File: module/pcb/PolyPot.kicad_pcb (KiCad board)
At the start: 2 copper layers, 50 x 50 mm, 42 parts, among them J1 V_BAT_1S, J10 I2C_TEST, J2 PROG/DEBUG, J3 HUMIDITY_CONN, J4 TOF_DIST_SENS, J5 M3, J6 M3, J7 M3, J8 M3, M1 DC_WATER_PUMP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

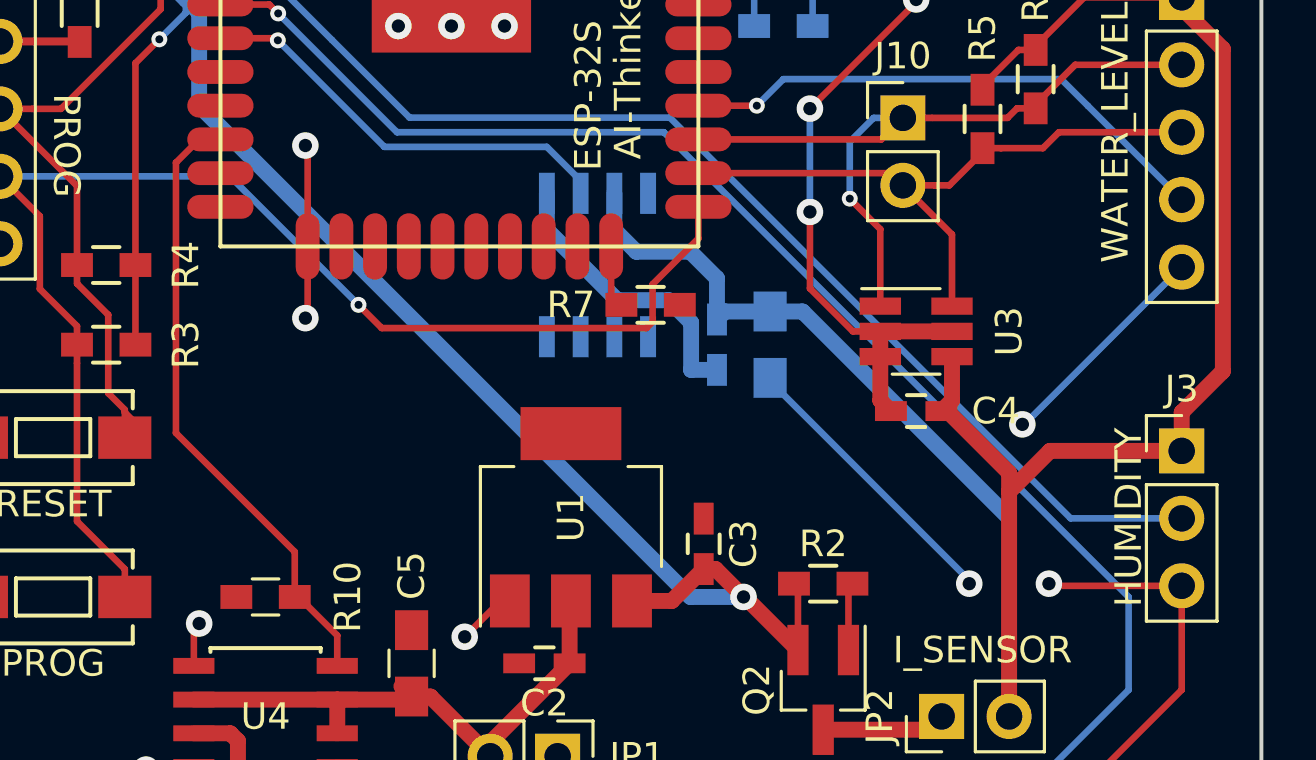
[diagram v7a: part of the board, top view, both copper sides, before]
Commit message: PCB: improve GND connection
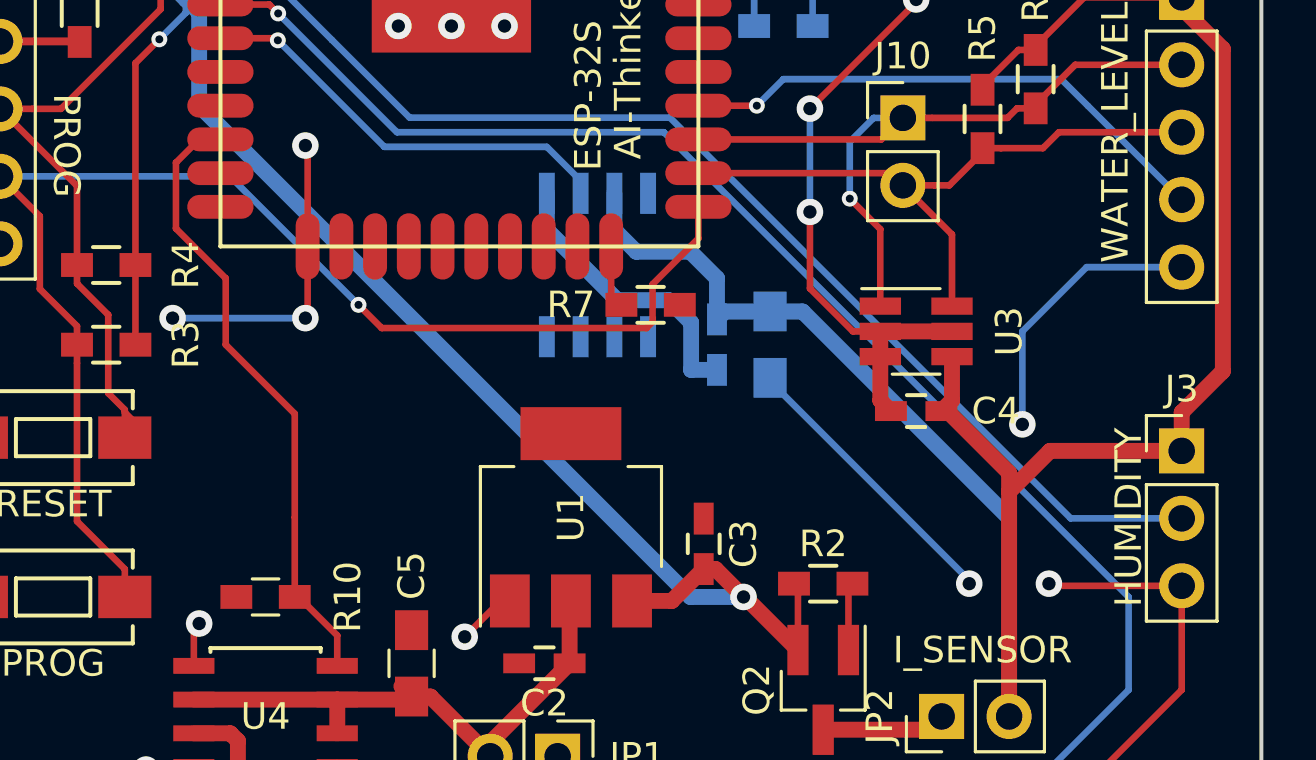
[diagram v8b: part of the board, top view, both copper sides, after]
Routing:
- net GND: track 150.4 -> 157.5 mm, vias 33 -> 34
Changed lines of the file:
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@@
     (thickness 1.6)
     (drawings 44)
-    (tracks 322)
+    (tracks 328)
     (zones 0)
     (modules 42)
@@
     (38 B.Mask user)
     (39 F.Mask user)
-    (40 Dwgs.User user)
+    (40 Dwgs.User user hide)
     (41 Cmts.User user)
     (42 Eco1.User user)
@@
     (user_trace_width 0.6)
     (trace_clearance 0.3)
-    (zone_clearance 0.508)
+    (zone_clearance 0.3)
     (zone_45_only no)
     (trace_min 0.2)
@@
   (gr_line (start 33.5 80) (end 76.5 80) (layer Edge.Cuts) (width 0.15))
   (gr_line (start 30 33.5) (end 30 76.5) (layer Edge.Cuts) (width 0.15))
+  (segment (start 44 57) (end 39 57) (width 0.25) (layer B.Cu) (net 1))
+  (via (at 39 57) (size 1) (drill 0.5) (layers F.Cu B.Cu) (net 1))
+  (segment (start 71 61) (end 71 57.5) (width 0.25) (layer B.Cu) (net 1))
+  (segment (start 77 55.08) (end 73.42 55.08) (width 0.25) (layer B.Cu) (net 1))
+  (segment (start 73.42 55.08) (end 71 57.5) (width 0.25) (layer B.Cu) (net 1))
   (segment (start 51.5 44) (end 56 44) (width 0.25) (layer B.Cu) (net 1))
   (via (at 56 44) (size 1) (drill 0.5) (layers F.Cu B.Cu) (net 1))
@@
   (segment (start 69 66.875) (end 69 67) (width 0.25) (layer B.Cu) (net 1))
   (via (at 69 67) (size 1) (drill 0.5) (layers F.Cu B.Cu) (net 1))
-  (segment (start 77 55.08) (end 71.08 61) (width 0.25) (layer B.Cu) (net 1))
-  (segment (start 71.08 61) (end 71 61) (width 0.25) (layer B.Cu) (net 1))
   (via (at 71 61) (size 1) (drill 0.5) (layers F.Cu B.Cu) (net 1))
   (segment (start 70 78) (end 68 76) (width 0.25) (layer F.Cu) (net 1))
@@
   (segment (start 54.365 52.3) (end 54.365 51.825) (width 0.25) (layer B.Cu) (net 16))
   (segment (start 54.365 51.825) (end 53.09001 50.55001) (width 0.25) (layer B.Cu) (net 16))
+  (segment (start 41 58) (end 43.6 60.6) (width 0.25) (layer F.Cu) (net 17))
+  (segment (start 39.12499 53.62499) (end 41 55.5) (width 0.25) (layer F.Cu) (net 17))
+  (segment (start 41 55.5) (end 41 58) (width 0.25) (layer F.Cu) (net 17))
+  (segment (start 40.8 50.27) (end 40 50.27) (width 0.25) (layer F.Cu) (net 17))
+  (segment (start 40 50.27) (end 39.12499 51.14501) (width 0.25) (layer F.Cu) (net 17))
+  (segment (start 39.12499 51.14501) (end 39.12499 53.62499) (width 0.25) (layer F.Cu) (net 17))
+  (segment (start 43.6 64.5) (end 43.6 67.5) (width 0.25) (layer F.Cu) (net 17))
+  (segment (start 43.6 60.6) (end 43.6 64.5) (width 0.25) (layer F.Cu) (net 17))
   (segment (start 45.2 70.095) (end 45.2 68.95) (width 0.25) (layer F.Cu) (net 17))
   (segment (start 45.2 68.95) (end 43.75 67.5) (width 0.25) (layer F.Cu) (net 17))
   (segment (start 43.75 67.5) (end 43.6 67.5) (width 0.25) (layer F.Cu) (net 17))
-  (segment (start 43.6 65.8) (end 43.6 67.5) (width 0.25) (layer F.Cu) (net 17))
-  (segment (start 40.8 50.27) (end 40 50.27) (width 0.25) (layer F.Cu) (net 17))
-  (segment (start 40 50.27) (end 39.12499 51.14501) (width 0.25) (layer F.Cu) (net 17))
-  (segment (start 39.12499 51.14501) (end 39.12499 61.32499) (width 0.25) (layer F.Cu) (net 17))
-  (segment (start 39.12499 61.32499) (end 43.6 65.8) (width 0.25) (layer F.Cu) (net 17))
   (segment (start 55.515 54.3) (end 55.515 56.115) (width 0.25) (layer F.Cu) (net 18))
   (segment (start 55.515 56.115) (end 55.9 56.5) (width 0.25) (layer F.Cu) (net 18))
@@
   (segment (start 61 49) (end 58.8 49) (width 0.25) (layer F.Cu) (net 27))
   (zone (net 1) (net_name GND) (layer F.Cu) (hatch edge 0.508)
-    (connect_pads (clearance 0.508))
-    (min_thickness 0.254)
+    (connect_pads (clearance 0.3))
+    (min_thickness 0.25)
     (fill yes (arc_segments 16) (thermal_gap 0.508) (thermal_bridge_width 0.508))
     (polygon
@@
   )
   (zone (net 1) (net_name GND) (layer B.Cu) (hatch edge 0.508)
-    (connect_pads (clearance 0.508))
-    (min_thickness 0.254)
+    (connect_pads (clearance 0.3))
+    (min_thickness 0.25)
     (fill yes (arc_segments 16) (thermal_gap 0.508) (thermal_bridge_width 0.508))
     (polygon
